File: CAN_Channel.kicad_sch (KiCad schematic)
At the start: 6 parts, among them K1 Relay_SPST-NO, Q1 AO3400A

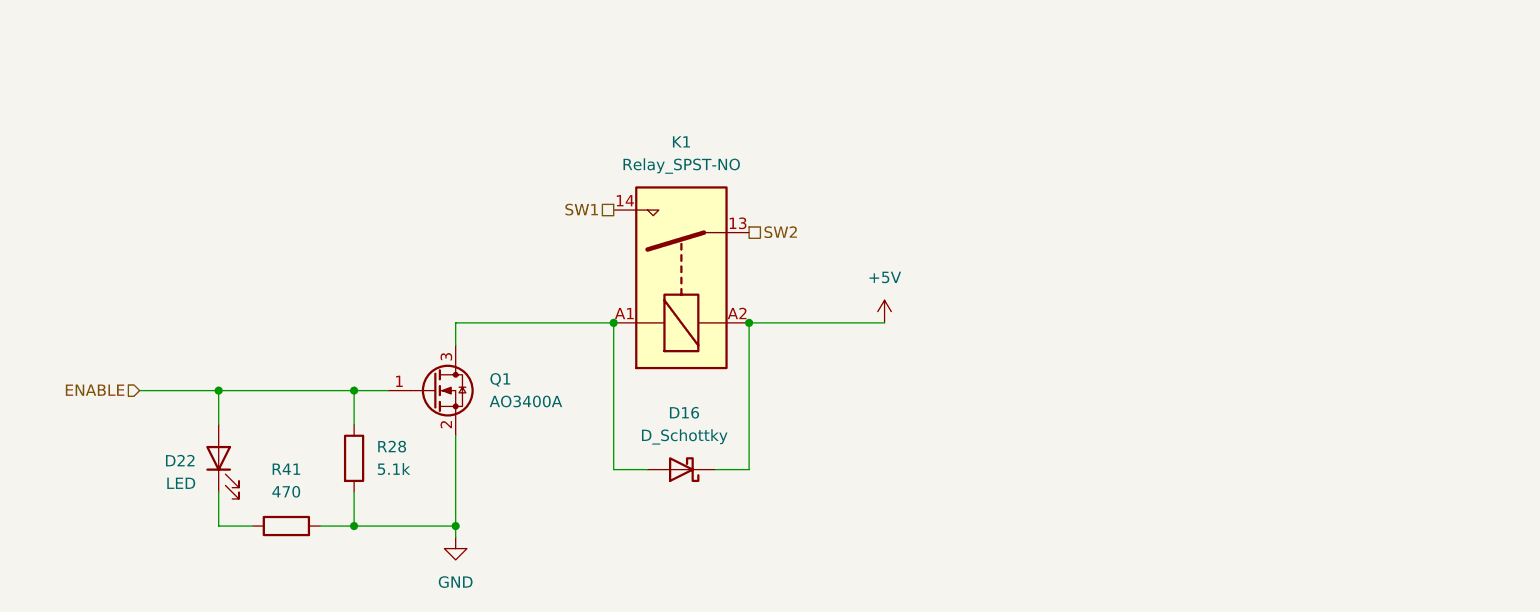
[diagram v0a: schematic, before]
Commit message: add MCU and power circuits
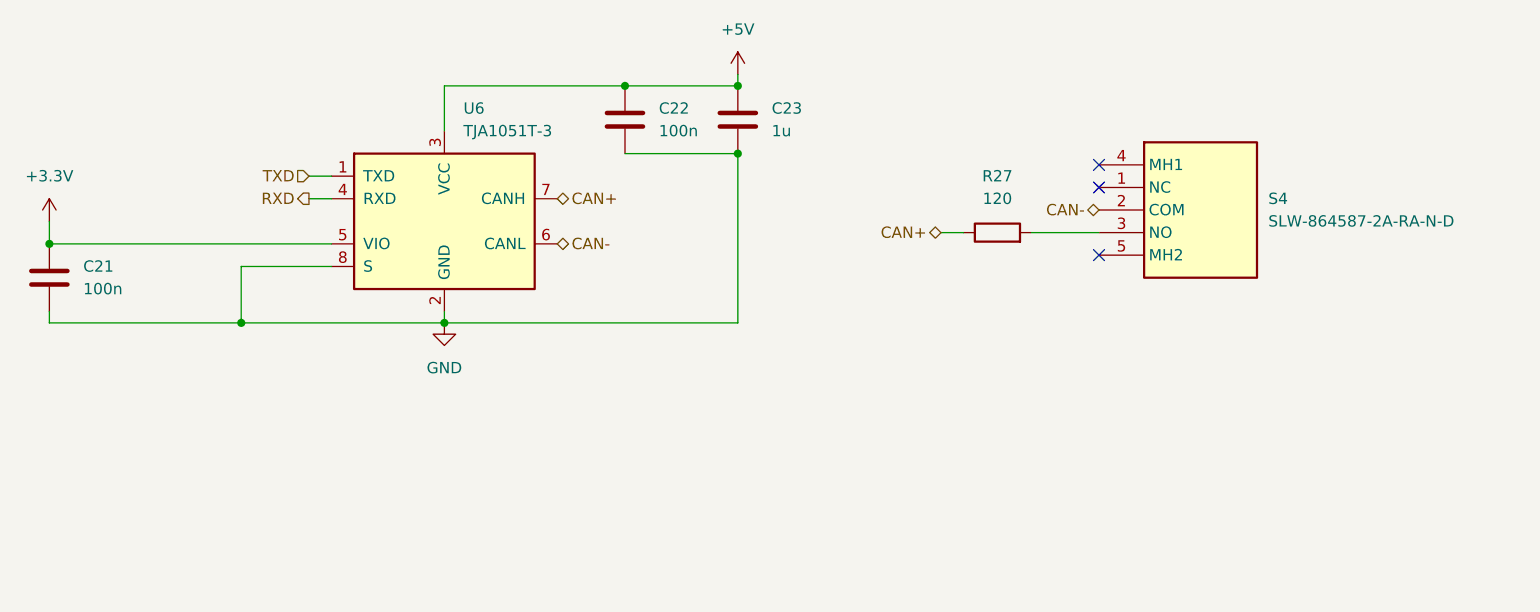
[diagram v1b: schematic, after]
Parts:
- removed D16: D_Schottky, Diode_SMD:D_SMA, symbol Device:D_Schottky
- removed D22: LED, LED_SMD:LED_0603_1608Metric_Pad1.05x0.95mm_HandSolder, symbol Device:LED
- removed K1: Relay_SPST-NO, Relay_THT:Relay_SPST_SANYOU_SRD_Series_Form_A, symbol Relay:Relay_SPST-NO
- removed Q1: AO3400A, Package_TO_SOT_SMD:SOT-23, symbol Transistor_FET:AO3400A
- removed R28: 5.1k, Resistor_SMD:R_0603_1608Metric_Pad0.98x0.95mm_HandSolder, symbol Device:R
- removed R41: 470, Resistor_SMD:R_0603_1608Metric_Pad0.98x0.95mm_HandSolder, symbol Device:R
- added C21, C22: 100n, Capacitor_SMD:C_0603_1608Metric_Pad1.08x0.95mm_HandSolder, symbol Device:C
- added C23: 1u, Capacitor_SMD:C_0603_1608Metric_Pad1.08x0.95mm_HandSolder, symbol Device:C
- added R27: 120, Resistor_SMD:R_0603_1608Metric_Pad0.98x0.95mm_HandSolder, symbol Device:R
- added S4: SLW-864587-2A-RA-N-D, SamacSys_Parts:SLW8645872ARAND, symbol SamacSys_Parts:SLW-864587-2A-RA-N-D
- added U6: TJA1051T-3, Package_SO:SOIC-8_3.9x4.9mm_P1.27mm, symbol Interface_CAN_LIN:TJA1051T-3
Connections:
- net +5V: now also C22.1, C23.1, U6.3 (VCC)
- net GND: now also C21.2, C22.2, C23.2, U6.2 (GND), U6.8 (S)
- new net: R27.2, S4.3 (NO)
- new net +3.3V: C21.1, U6.5 (VIO)
- new net CAN+: R27.1, U6.7 (CANH)
- new net CAN-: S4.2 (COM), U6.6 (CANL)
- new net RXD: U6.4 (RXD)
- new net TXD: U6.1 (TXD)
- no-connect marks 0 -> 3
